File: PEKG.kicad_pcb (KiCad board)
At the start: 2 copper layers, 90 x 60 mm, 130 parts, among them J1 AudioJack4, J2 AudioJack3_SwitchTR, Q10 AO3401A, Q13 AO3400A, Q14 AO3400A, Q3 AO3400A, Q5 AO3400A, Q8 AO3401A, SW1 SW_DPDT_x2, U1 OP07, U11 AP9101CK6, U2 ESP32-S3-ZERO, U3 OP07, U4 NE5532, U5 NE5532, U6 BQ21040DBV, U7 74HC14, U8 74HC14

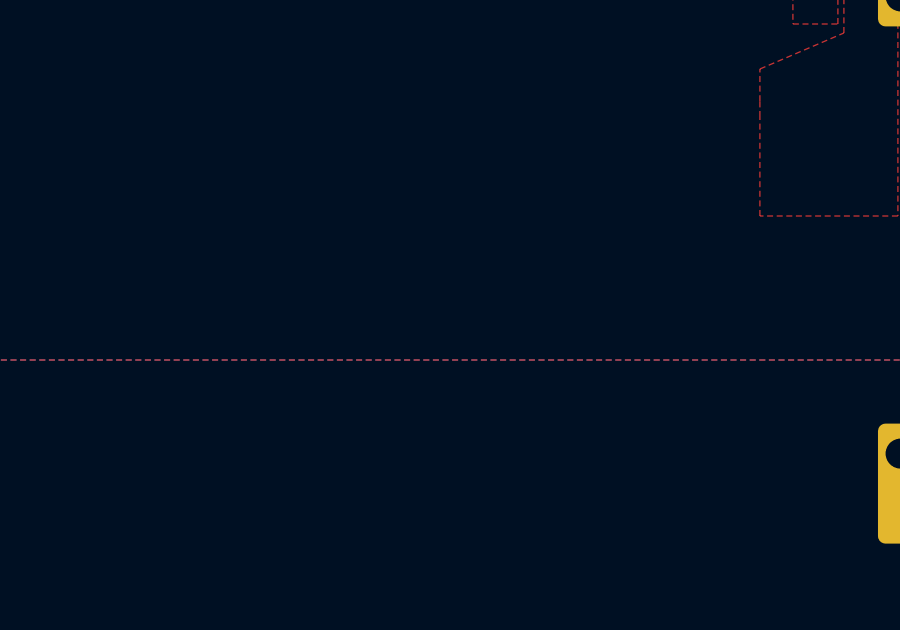
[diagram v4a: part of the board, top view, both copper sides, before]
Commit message: connected SD and ESP
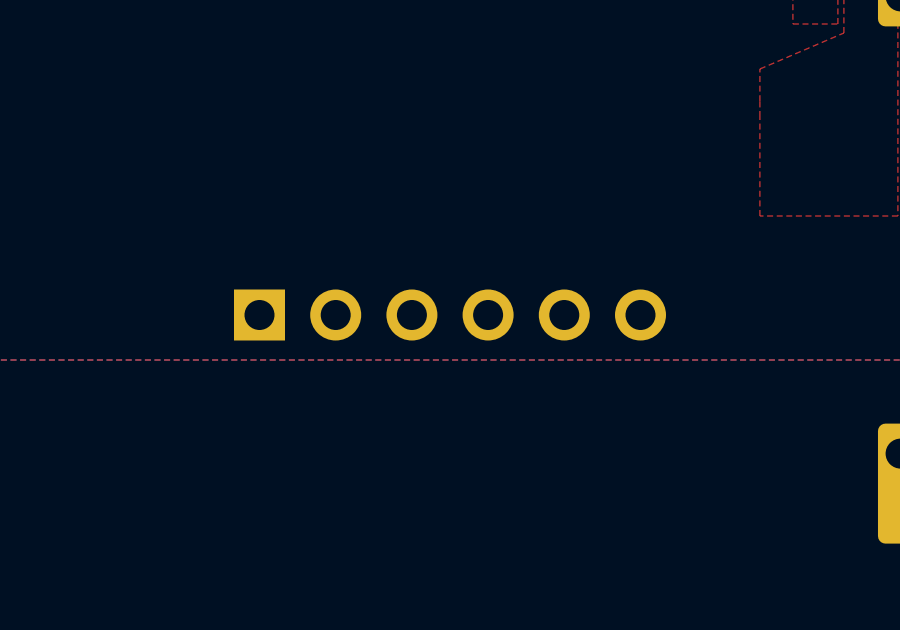
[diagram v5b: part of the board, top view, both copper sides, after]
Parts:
- added J3: Micro_SD_Card_Module, PEKG:Micro_SD_Card_Module, B.Cu at (147.2, 143.5)
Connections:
- U2 pad 10: unconnected-(U2-GP10-Pad10) -> /MCU/CS
- U2 pad 11: unconnected-(U2-GP11-Pad11) -> /MCU/MOSI
- U2 pad 12: unconnected-(U2-GP12-Pad12) -> /MCU/CLK
- U2 pad 13: unconnected-(U2-GP13-Pad13) -> /MCU/MISO
- U2 pad 3V3: unconnected-(U2-3V3(OUT)-Pad3V3) -> +3V3
- U7 pad 1: unconnected-(U7-Pad1) -> (no net)
- U7 pad 10: (no net) -> NMOS_GATE
- U7 pad 11: (no net) -> Net-(D11-K)
- U7 pad 12: (no net) -> NMOS_GATE
- U7 pad 13: (no net) -> Net-(D11-K)
- U7 pad 2: unconnected-(U7-Pad2) -> (no net)
- U7 pad 3: (no net) -> Net-(D12-A)
- U7 pad 4: (no net) -> PMOS_GATE
- U7 pad 5: (no net) -> Net-(D12-A)
- U7 pad 6: (no net) -> PMOS_GATE
- U7 pad 8: (no net) -> CLK
- U7 pad 9: (no net) -> Net-(D10-A)
- U8 pad 1: Net-(D10-A) -> Net-(D12-A)
- U8 pad 14: (no net) -> V_{cc}
- U8 pad 2: CLK -> PMOS_GATE
- U8 pad 7: (no net) -> 0

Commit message: updated form factor and placment
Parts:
- removed C47: 10u, Capacitor_SMD:C_0603_1608Metric_Pad1.08x0.95mm_HandSolder
- removed D6: LED, LED_THT:LED_D3.0mm_FlatTop
- removed R1: 10k, Resistor_SMD:R_0603_1608Metric_Pad0.98x0.95mm_HandSolder
- removed SW1: SW_DPDT_x2, PEKG:DPDT_bigger
- added C8: 100n, Capacitor_SMD:C_0603_1608Metric_Pad1.08x0.95mm_HandSolder, F.Cu at (132.9, 137.3)
- added D5: RED_LED, LED_SMD:LED_0805_2012Metric_Pad1.15x1.40mm_HandSolder, F.Cu at (-22.9, 8.16)
- added R7: 10k, Resistor_SMD:R_0603_1608Metric_Pad0.98x0.95mm_HandSolder, F.Cu at (132.9, 139.8)
- added SW2: SW_DPDT_x2, PEKG:SW_EG1271, B.Cu at (125.5, 123.8)
- D3: value LED -> GREEN_LED; footprint LED_SMD:LED_0603_1608Metric_Pad1.05x0.95mm_HandSolder -> LED_SMD:LED_0805_2012Metric_Pad1.15x1.40mm_HandSolder
- J2, R25: moved to B.Cu
- J3: footprint PEKG:Micro_SD_Card_Module -> PEKG:Micro_SD_Card_Module_UpsideDown_SMD
- U2: footprint PEKG:MODULE_ESP32-S3-ZERO -> PEKG:MODULE_ESP32-S3-ZERO_SMD
- moved D3 376.9 mm to (-22.9, 5.12)
- moved R25 276.5 mm to (146.8, 110.7)
- moved J2 220.0 mm to (103.3, 128.5), turned to 90 degrees
- moved U2 32.0 mm to (147.5, 133.6), turned to 0 degrees
- moved J3 17.4 mm to (163.4, 137.0), turned to 0 degrees
- moved H2 15.0 mm to (105.0, 140.0)
- moved H4 15.0 mm to (185.0, 140.0)
- moved BT2 8.50 mm to (145.0, 110.5), turned to 180 degrees
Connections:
- D3 pad 1: GND -> unconnected-(D3-K-Pad1)
- D3 pad 2: Net-(D3-A) -> unconnected-(D3-A-Pad2)
- U2 pad 1: unconnected-(U2-GP1-Pad1) -> Net-(U2-GP1)
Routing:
- removed copper zone on F.Cu, net (none)
- removed copper zone on F.Cu, net VBAT
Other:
- board size 90 x 60 mm -> 90 x 45 mm

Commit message: ADC, levels
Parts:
- removed C48: 10u, Capacitor_SMD:C_0603_1608Metric_Pad1.08x0.95mm_HandSolder
- removed R28, R29, R42, R43, R51: 100k, Resistor_SMD:R_0603_1608Metric_Pad0.98x0.95mm_HandSolder
- removed U8: 74HC14, Package_SO:SOIC-14_3.9x8.7mm_P1.27mm
- added C9: 10u, Capacitor_SMD:C_0603_1608Metric_Pad1.08x0.95mm_HandSolder, F.Cu at (142.8, 162.1)
- added R1: 1k, Resistor_SMD:R_0603_1608Metric_Pad0.98x0.95mm_HandSolder, F.Cu at (149.2, 162.1)
- added R14: 100k, Resistor_SMD:R_0603_1608Metric_Pad0.98x0.95mm_HandSolder, F.Cu at (142.8, 164.6)
- added R15: 1k, Resistor_SMD:R_0603_1608Metric_Pad0.98x0.95mm_HandSolder, F.Cu at (142.8, 167.1)
- added R16: 1k, Resistor_SMD:R_0603_1608Metric_Pad0.98x0.95mm_HandSolder, F.Cu at (142.8, 169.6)
- added TP1: TestPoint_Alt, Connector_PinHeader_2.54mm:PinHeader_1x01_P2.54mm_Vertical, F.Cu at (138.3, 163.1)
- added TP15: TestPoint_Alt, Connector_PinHeader_2.54mm:PinHeader_1x01_P2.54mm_Vertical, F.Cu at (138.3, 172.3)
- added TP2: TestPoint_Alt, Connector_PinHeader_2.54mm:PinHeader_1x01_P2.54mm_Vertical, F.Cu at (138.3, 167.7)
- J2: value AudioJack3_SwitchTR -> EKG input
- R12: value 10k -> 1k
- R2: value 100 -> 200k
- R4: value 200k -> 1k
- TP14: value TestPoint -> TestPoint_Alt; footprint TestPoint:TestPoint_Pad_D3.0mm -> Connector_PinHeader_2.54mm:PinHeader_1x01_P2.54mm_Vertical
- moved D3 195.6 mm to (100.0, 157.4)
- moved D5 195.6 mm to (100.0, 160.4)
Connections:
- net /LA_IN renamed /Amplifier/LA_IN
- net /RA_IN renamed /Amplifier/RA_IN
- net GAIN_50 renamed OUTPUT
- C32 pad 1: /BOTTOM -> /Amplifier/BOTTOM
- C33 pad 2: /TOP -> /Amplifier/TOP
- D3 pad 1: unconnected-(D3-K-Pad1) -> 0
- D3 pad 2: unconnected-(D3-A-Pad2) -> Net-(D3-A)
- R12 pad 1: GND -> /Amplifier/TOP
- R12 pad 2: Net-(C48-Pad1) -> Net-(U5A-+)
- R2 pad 1: Net-(C48-Pad2) -> 3V3
- R2 pad 2: FIL_OUT -> OUTPUT_ADC
- R3 pad 1: GND -> OUTPUT_ADC
- R3 pad 2: Net-(U4B-+) -> GND
- R4 pad 1: V_{cc} -> /Amplifier/BOTTOM
- R4 pad 2: Net-(U4B-+) -> Net-(U5A--)
- R44 pad 2: /TOP -> /Amplifier/TOP
- R45 pad 1: /BOTTOM -> /Amplifier/BOTTOM
- R49 pad 2: /TOP -> /Amplifier/TOP
- R50 pad 1: /BOTTOM -> /Amplifier/BOTTOM
- R53 pad 1: /BOTTOM -> /Amplifier/BOTTOM
- R54 pad 1: /TOP -> /Amplifier/TOP
- R7 pad 2: /MCU/ADC1 -> OUTPUT_ADC
- TP5 pad 1: /TOP -> /Amplifier/TOP
- TP6 pad 1: /BOTTOM -> /Amplifier/BOTTOM
- U1 pad 6: /TOP -> /Amplifier/TOP
- U3 pad 6: /BOTTOM -> /Amplifier/BOTTOM
- U7 pad 1: (no net) -> Net-(D12-A)
- U7 pad 14: (no net) -> V_{cc}
- U7 pad 2: (no net) -> PMOS_GATE
- U7 pad 7: (no net) -> 0
